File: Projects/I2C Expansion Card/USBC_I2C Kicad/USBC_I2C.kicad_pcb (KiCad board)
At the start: 2 copper layers, 26 x 30 mm, 26 parts, among them SW1 SW_DIP_x04, U1 MCP2221AxSL

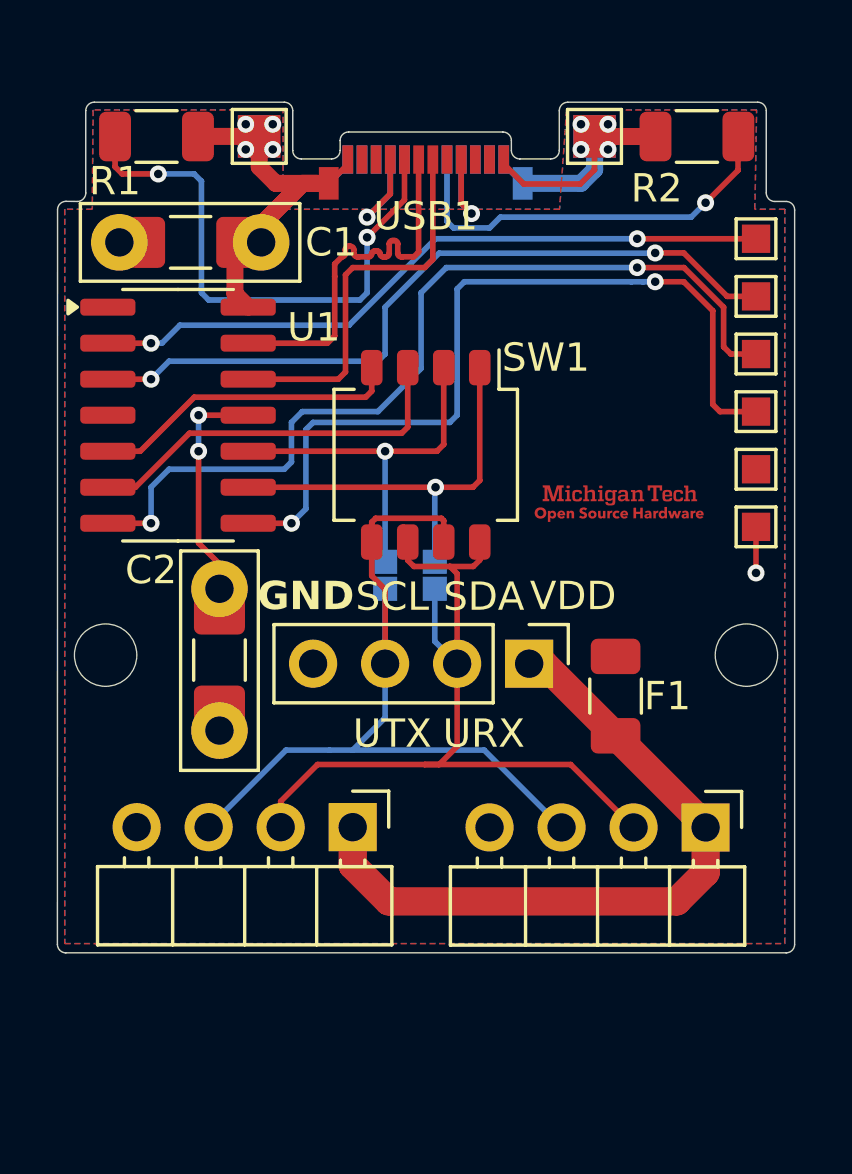
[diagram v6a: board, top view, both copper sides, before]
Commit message: Added silkscreen for switch pinouts
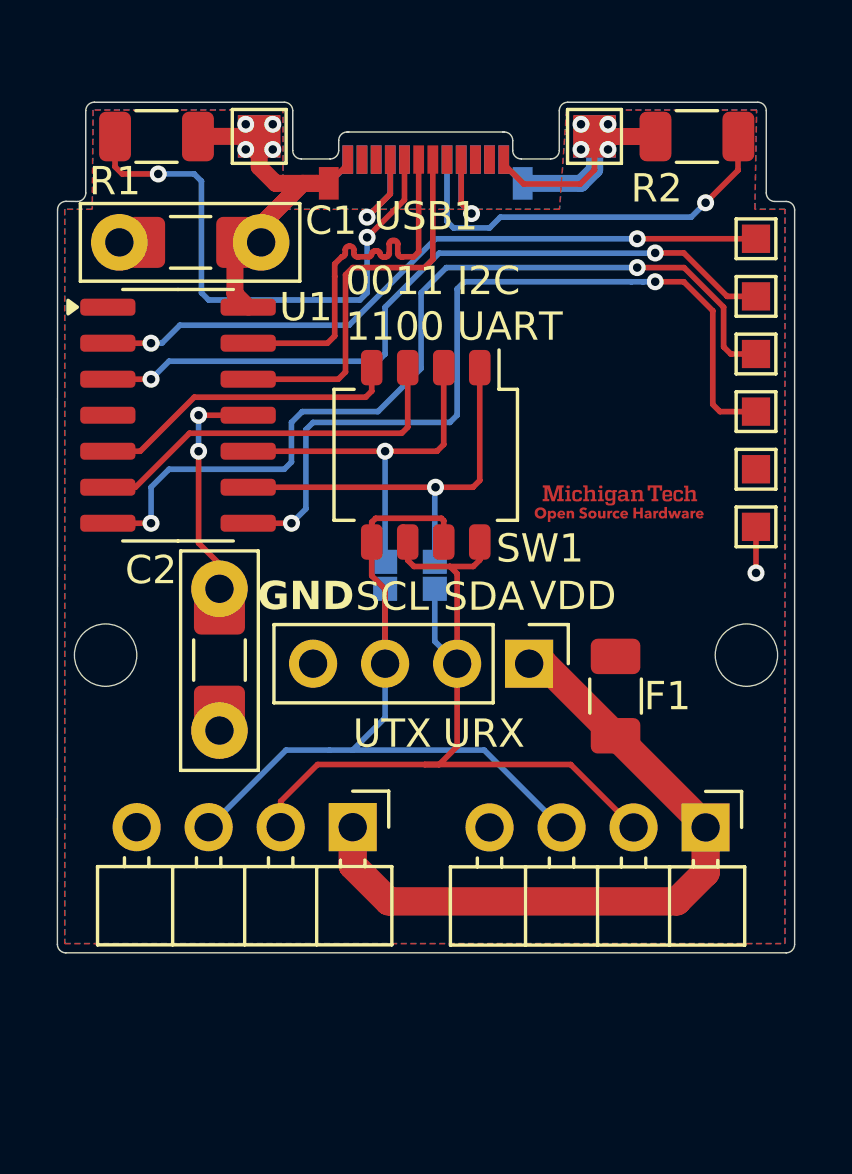
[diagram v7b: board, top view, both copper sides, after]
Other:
- outline, holes or cut-outs redrawn
- board text added: "0011 I2C 1100 UART"
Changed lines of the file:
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@@
 		(tags "SMD DIP Switch SPST Slide 6.15mm 242mil")
 		(property "Reference" "SW1"
-			(at -3.429 -4.235 180)
+			(at 3.302 -4.028 180)
 			(layer "F.SilkS")
 			(effects
@@
 		(tags "capacitor handsolder")
 		(property "Reference" "C1"
-			(at -4.953 0 180)
+			(at -4.953 0.762 180)
 			(layer "F.SilkS")
 			(effects
@@
 		(tags "SOIC SO")
 		(property "Reference" "U1"
-			(at 4.7894 -3.0988 0)
+			(at 4.51 -3.81 0)
 			(layer "F.SilkS")
 			(effects
@@
 	)
 	(gr_arc
-		(start 99.53 58.21)
-		(mid 99.742132 58.297868)
-		(end 99.83 58.51)
+		(start 99.577868 58.21)
+		(mid 99.79 58.297868)
+		(end 99.877868 58.51)
 		(stroke
 			(width 0.05)
@@
 	)
 	(gr_line
-		(start 93.79 58.51)
-		(end 93.79 58.86)
+		(start 93.74 58.51)
+		(end 93.74 58.86)
 		(stroke
 			(width 0.05)
@@
 		(layer "Edge.Cuts")
 	)
-	(gr_line
-		(start 92.42 59.16)
-		(end 93.49 59.16)
-		(stroke
-			(width 0.05)
-			(type default)
-		)
-		(layer "Edge.Cuts")
-	)
 	(gr_arc
 		(start 91.82 57.16)
@@
 	)
 	(gr_line
-		(start 101.22 59.16)
-		(end 100.13 59.16)
-		(stroke
-			(width 0.05)
-			(type default)
-		)
-		(layer "Edge.Cuts")
-	)
-	(gr_line
 		(start 108.82 60.36)
 		(end 108.82 57.46)
@@
 	)
 	(gr_line
-		(start 99.83 58.51)
-		(end 99.83 58.86)
+		(start 100.177868 59.16)
+		(end 101.22 59.16)
+		(stroke
+			(width 0.05)
+			(type default)
+		)
+		(layer "Edge.Cuts")
+	)
+	(gr_line
+		(start 99.877868 58.51)
+		(end 99.877868 58.86)
 		(stroke
 			(width 0.05)
@@
 	)
 	(gr_arc
-		(start 93.79 58.51)
-		(mid 93.877868 58.297868)
-		(end 94.09 58.21)
+		(start 93.74 58.51)
+		(mid 93.827868 58.297868)
+		(end 94.04 58.21)
 		(stroke
 			(width 0.05)
@@
 	)
 	(gr_line
+		(start 92.42 59.16)
+		(end 93.44 59.16)
+		(stroke
+			(width 0.05)
+			(type default)
+		)
+		(layer "Edge.Cuts")
+	)
+	(gr_line
 		(start 84.82 57.46)
 		(end 84.82 60.36)
@@
 	)
 	(gr_arc
-		(start 100.13 59.16)
-		(mid 99.917868 59.072132)
-		(end 99.83 58.86)
+		(start 100.177868 59.16)
+		(mid 99.965736 59.072132)
+		(end 99.877868 58.86)
 		(stroke
 			(width 0.05)
@@
 		(layer "Edge.Cuts")
 	)
+	(gr_line
+		(start 94.04 58.21)
+		(end 94.09 58.21)
+		(stroke
+			(width 0.05)
+			(type default)
+		)
+		(layer "Edge.Cuts")
+	)
 	(gr_arc
-		(start 93.79 58.86)
-		(mid 93.702132 59.072132)
-		(end 93.49 59.16)
+		(start 93.74 58.86)
+		(mid 93.652132 59.072132)
+		(end 93.44 59.16)
 		(stroke
 			(width 0.05)
@@
 		(start 101.52 58.86)
 		(end 101.52 57.46)
+		(stroke
+			(width 0.05)
+			(type default)
+		)
+		(layer "Edge.Cuts")
+	)
+	(gr_line
+		(start 99.53 58.21)
+		(end 99.577868 58.21)
 		(stroke
 			(width 0.05)
@@
 		)
 	)
+	(gr_text "\n0011 I2C\n1100 UART"
+		(at 93.98 65.659 0)
+		(layer "F.SilkS")
+		(effects
+			(font
+				(size 1 1)
+				(thickness 0.15)
+			)
+			(justify left bottom)
+		)
+	)
